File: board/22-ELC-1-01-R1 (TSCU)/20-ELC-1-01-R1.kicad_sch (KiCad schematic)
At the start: 8 parts, among them J1 Conn_01x116, J2 Conn_01x02_Female, J3 Conn_01x06, J4 Conn_01x02, J5 Conn_01x02, J6 Conn_01x06, J7 Conn_01x01

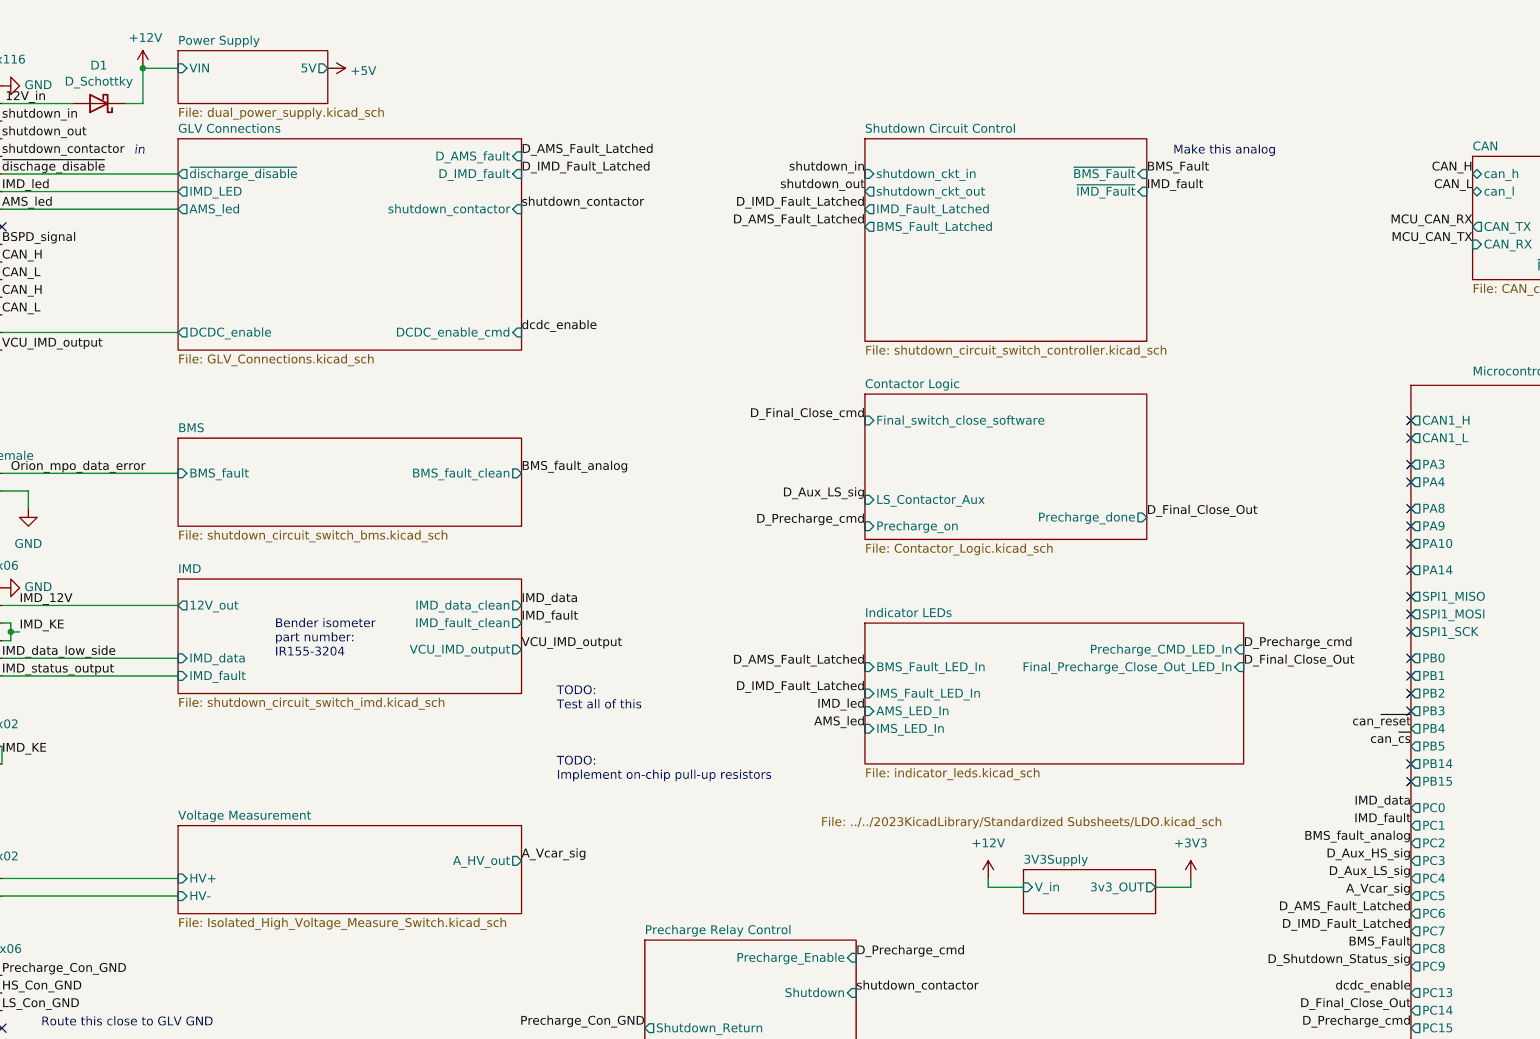
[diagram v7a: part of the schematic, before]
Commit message: Added standard VRM and more internal connections
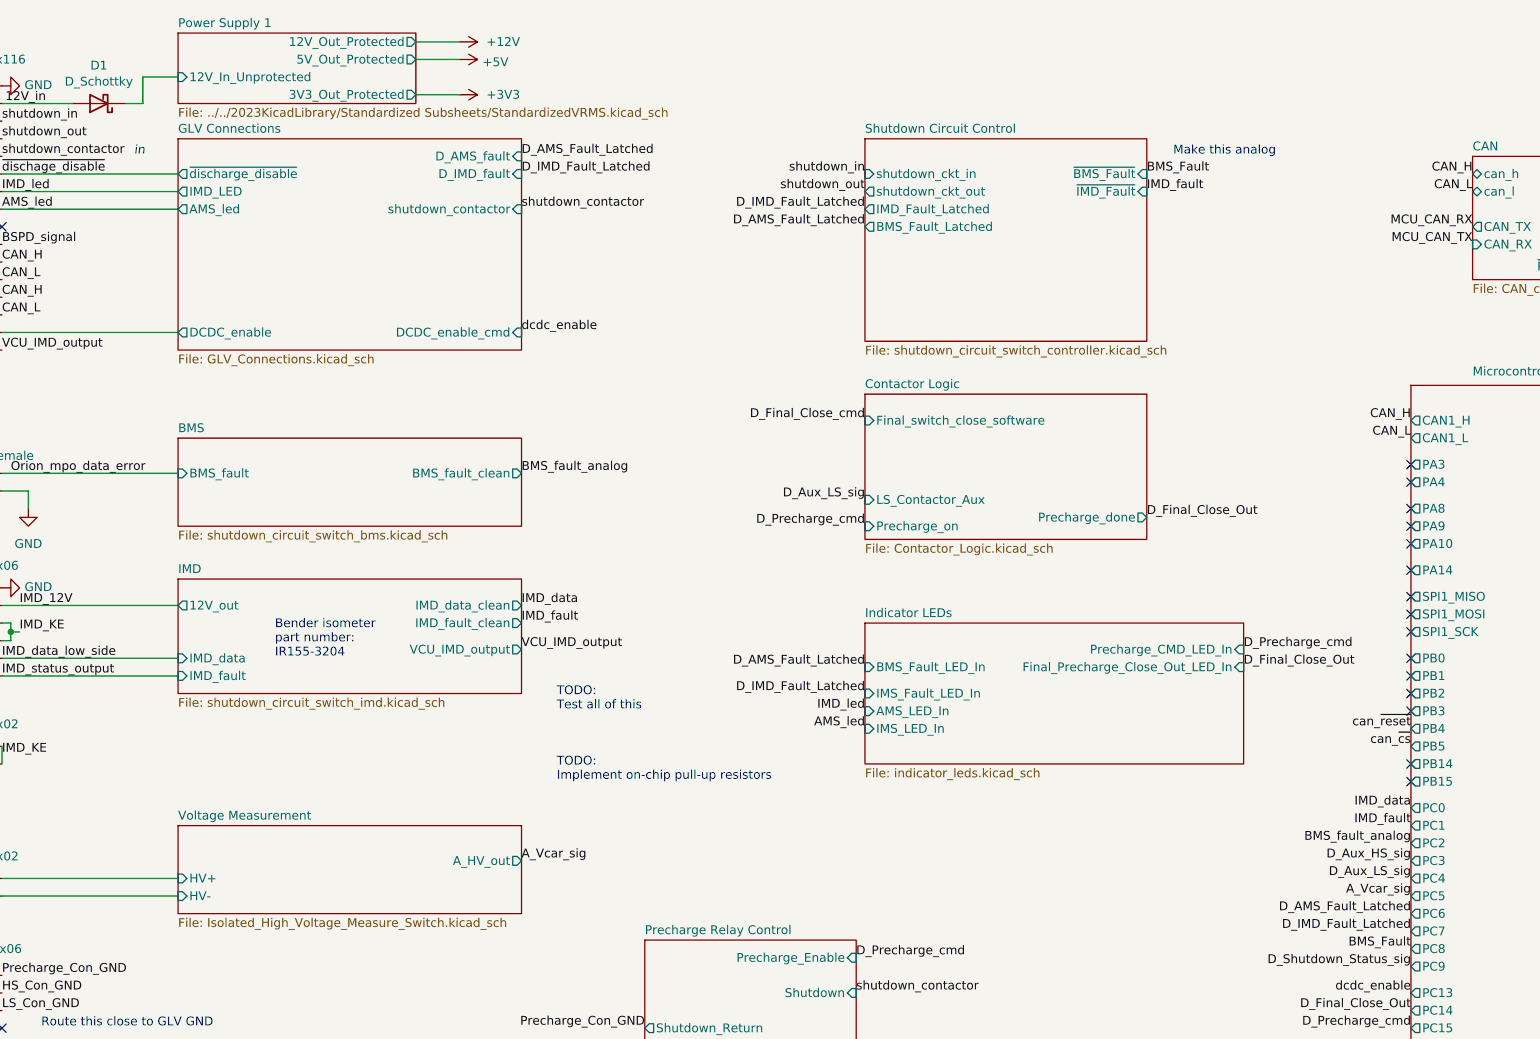
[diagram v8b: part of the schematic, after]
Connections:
- net +12V: no longer D1.1 (K)
- new net Power Supply 1/12V_In_Unprotected: D1.1 (K)
- no-connect marks 33 -> 31
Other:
- removed sheet 3V3Supply
- removed sheet Power Supply
- added sheet Power Supply 1 (../../2023KicadLibrary/Standardized Subsheets/StandardizedVRMS.kicad_sch)
